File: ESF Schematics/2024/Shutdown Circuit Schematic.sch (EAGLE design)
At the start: 32 parts, among them J1 CONNECTOR-1_6MM2, J10 CONNECTOR-1_CT2242-2, J11 CONNECTOR-3_XXC106-EV-P3Z, J15 CONNECTOR-3_NEMA-5-20, J16 CONNECTOR-3_NEMA-5-20, J17 CONNECTOR-2_, J18 CONNECTOR-2_, J2 CONNECTOR-1_LCAX2-14F-E, J3 CONNECTOR-1_6MM2, J4 CONNECTOR-1_LCAX2-14F-E, J5 CONNECTOR-3_XXC106-EV-P3Z, J6 RING_TERMINAL_19054-0042, J7 RING_TERMINAL_19054-0042, J8 CONNECTOR-3_NEMA-5-20, J9 CONNECTOR-1_CT2242-2

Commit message: num num
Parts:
- removed A1: REMOTE_POWER_CONTROL_RPC-20-SCD, HyTechSymbolsTemp:REMOTE_POWER_CONTROL_RPC-20-SCD
- removed A2: CHARGER_HK-J-H650-12, HyTechSymbols:CHARGER_HK-J-H650-12
- removed A3: INLINE_GFCI_GFM20-3WC, HyTechSymbolsTemp:INLINE_GFCI_GFM20-3WC
- removed F4: 1A, HyTechSymbolsTemp:FUSE
- removed J10, J9: CONNECTOR-1_CT2242-2, HyTechSymbolsTemp:CONNECTOR-1_CT2242-2
- removed J11, J5: CONNECTOR-3_XXC106-EV-P3Z, HyTechSymbols:CONNECTOR-3_XXC106-EV-P3Z
- removed J15, J16, J8: CONNECTOR-3_NEMA-5-20, HyTechSymbolsTemp:CONNECTOR-3_NEMA-5-20
- removed J17, J18: CONNECTOR-2_, HyTechSymbols:CONNECTOR-2_XXC104-EV-P1ZA
- removed J2, J4: CONNECTOR-1_LCAX2-14F-E, HyTechSymbols:CONNECTOR-1_LCAX2-14F-E
- removed J3: CONNECTOR-1_6MM2, HyTechSymbols:CONNECTOR-1_6MM2
- removed J6, J7: RING_TERMINAL_19054-0042, HyTechSymbols:RING_TERMINAL_19054-0042
- removed R1: 15k, HyTechSymbolsTemp:RESISTOR
- removed U$7: RING_TERMINAL_19054-0042, HyTechSymbolsTemp:RING_TERMINAL_19054-0042
- added AIR+, AIR-: RELAY_SPST_NO_, HyTechSymbols:RELAY_SPST_NO_
- added AMS_RELAY, BOTS_SENSE_RELAY, BSPD_RELAY, IMD_RELAY, SOFTWARE_SHDN_RELAY: RELAY_DPDT_RT424024, HyTechSymbols:RELAY_DPDT_RT424024
- added D1, D10, D2, D3, D4, D5, D6, D7, D8, D9: DIODE, HyTechSymbolsTemp:DIODE
- added DISCHARGE: RELAY_SPST_NC_DBR72410, HyTechSymbols:RELAY_SPST_NC_DBR72410
- added DISCHARGE_RES, DISCHARGE_RES1, DISCHARGE_RES2: 15k, HyTechSymbolsTemp:RESISTOR
- added F1: 10A, HyTechSymbolsTemp:FUSE
- added F6: 1A, HyTechSymbolsTemp:FUSE
- added GLV_BATTERY: BATTERY, HyTechSymbols:BATTERY
- added LATCHING_BUTTON: BUTTON_NO_LP9, HyTechSymbolsTemp:BUTTON_NO_LP9
- added MAIN_FUSE: 125A, HyTechSymbolsTemp:FUSE
- added PACK+OPTOISOLATOR: RELAY_SOLIDSTATE_NO_, HyTechSymbolsTemp:RELAY_SOLIDSTATE_NO_
- added PRECHARGE: RELAY_SPST_NO_DAR72410, HyTechSymbols:RELAY_SPST_NO_DAR72410
- added PRECHARGE_RES, PRECHARGE_RES1: 1.5k, HyTechSymbolsTemp:RESISTOR
- added Q1, Q2: MOSFET_N-CHANNEL, HyTechSymbolsTemp:MOSFET_N-CHANNEL
- added R3: 3.3k, HyTechSymbolsTemp:RESISTOR
- added S10, S11, S12, S13, S6, S7: SWITCH_SPST_, HyTechSymbols:SWITCH_SPST_
- added S3: SWITCH_SPST_27MM_STOP, HyTechSymbols:SWITCH_SPST_27MM_STOP
- added S4, S5: SWITCH_SPST_40MM_STOP, HyTechSymbols:SWITCH_SPST_40MM_STOP
- added S8, S9: SWITCH_SPST_35-210-100-R-900, HyTechSymbols:SWITCH_SPST_35-210-100-R-900
- added U$10: BENDER_IR155-3204, HyTechSymbols:BENDER_IR155-3204
- added U$12, U$13, U$14: SEGMENT, HyTechSymbols:SEGMENT
- added U$17: PRECHARGER, HyTechSymbolsTemp:PRECHARGER
- added U$2, U$20, U$21, U$22, U$23, U$24, U$25, U$34, U$35, U$36, U$37: MAINTENANCE_PLUG_104742-2, HyTechSymbolsTemp:MAINTENANCE_PLUG_104742-2
- added U$38, U$39, U$40: RING_TERMINAL_19054-0042, HyTechSymbolsTemp:RING_TERMINAL_19054-0042
- added U1, U2: LOGICGATE_INVERTER, HyTechSymbolsTemp:LOGICGATE_INVERTER
- F3: value 175A -> 3A
- J1: value CONNECTOR-1_6MM2 -> CONNECTOR-2_HVP800; device HyTechSymbols:CONNECTOR-1_6MM2 -> HyTechSymbols:CONNECTOR-2_HVP800
- R2: value 15k -> 39
- S1: value SWITCH_SPST_ -> SWITCH_SPST_INERTIA_SWITCH; device HyTechSymbols:SWITCH_SPST_ -> HyTechSymbols:SWITCH_SPST_INERTIA_SWITCH; MPN AIR+ -> (none)
- S2: MPN AIR- -> BOTS
- U$1, U$4: value CONNECTOR-2_HVP800 -> SEGMENT; device HyTechSymbols:CONNECTOR-2_HVP800 -> HyTechSymbols:SEGMENT
- U$15: value CHARGER_CONTROLLER -> SEGMENT; device HyTechSymbolsTemp:CHARGER_CONTROLLER -> HyTechSymbols:SEGMENT
- U$3: value CONNECTOR-3_XXC106-EV-P3Z -> MAINTENANCE_PLUG_104742-2; device HyTechSymbols:CONNECTOR-3_XXC106-EV-P3Z -> HyTechSymbolsTemp:MAINTENANCE_PLUG_104742-2
- U$5: value BENDER_IR155-3204 -> MAINTENANCE_PLUG_104742-2; device HyTechSymbols:BENDER_IR155-3204 -> HyTechSymbolsTemp:MAINTENANCE_PLUG_104742-2
- U$6: value RING_TERMINAL_19054-0042 -> MAINTENANCE_PLUG_104742-2; device HyTechSymbolsTemp:RING_TERMINAL_19054-0042 -> HyTechSymbolsTemp:MAINTENANCE_PLUG_104742-2
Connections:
- removed net CHARGER_CONTROLLER_CANH: A2.CANH, U$15.CANH
- removed net CHARGER_CONTROLLER_CANL: A2.CANL, U$15.CANL
- removed net N$22 (its old number): A1.HOTIN, J15.1
- removed net N$27: R2.1, U$6.P$2
- removed net N$28: A3.HOT_OUT, J8.1
- removed net N$30: A3.GND_IN, J16.3
- removed net OKHS: U$5.OKHS
- new net +5V: U$17.VDD
- new net AMS_OK: AMS_RELAY.COIL+, D7.C
- new net BOTS_SENSE: BOTS_SENSE_RELAY.COIL+, D2.C, IMD_RELAY.6, S2.O
- new net BSPD_OK: BSPD_RELAY.COIL+, D9.C
- new net GLV_SYSTEMS: F3.1, S9.S
- new net IMD_OK: D10.C, IMD_RELAY.COIL+, U$10.OKHS
- new net N$12: S4.O, S5.P
- new net N$13: S5.O, S7.P
- new net N$16: BOTS_SENSE_RELAY.3, BOTS_SENSE_RELAY.COIL-, D1.A, D2.A
- new net N$17: S12.P, S13.S
- new net N$18: S1.O, S11.P
- new net N$34: U$14.+, U$23.1
- new net N$36: U$15.+, U$25.1
- new net N$37: U$34.P$1, U$35.P$1
- new net N$38: AIR+.CONTACT2, U$34.1
- new net N$39: PACK+OPTOISOLATOR.CONTROL+, R3.1
- new net N$40: PACK+OPTOISOLATOR.CONTACT1, R2.2
- new net N$42: BSPD_RELAY.5, SOFTWARE_SHDN_RELAY.6
- new net N$43: U$20.P$1, U$21.P$1
- new net N$44: U$22.P$1, U$23.P$1
- new net N$45: U$24.P$1, U$25.P$1
- new net N$46: U$36.P$1, U$37.P$1
- new net N$47: AIR-.CONTACT1, U$37.1
- new net N$48: F6.2, U$38.P$1
- new net N$50: F5.2, U$39.P$1
- new net N$51: S6.P, S7.S
- new net N$52: Q2.G, U2.!IN
- new net N$53: AIR+.COIL+, Q2.D
- new net N$54: U$1.+, U$3.1
- new net N$55: U$2.P$1, U$3.P$1
- new net N$56: U$36.1, U$4.-
- new net N$57: U$4.+, U$6.1
- new net N$58: U$5.P$1, U$6.P$1
- new net N$59: S12.S, S3.P
- new net PACK+: PACK+OPTOISOLATOR.CONTACT2, PRECHARGE.CONTACT1, U$12.+, U$35.1, U$40.P$2
- new net PACK+FUSED: R2.1, U$17.PACK+
- new net PRECHARGE_OK: PRECHARGE.COIL+, Q1.D, U1.IN
- new net SOFTWARE_OK: D8.C, SOFTWARE_SHDN_RELAY.COIL+
- new net TS+UNFUSED: AIR+.CONTACT1, DISCHARGE.CONTACT1, J1.1, PRECHARGE_RES.2, PRECHARGE_RES1.2
- net +12V: now also U$10.+12V; no longer U$5.+12V
- net GND: now also AIR-.COIL+, AMS_RELAY.4, BOTS_SENSE_RELAY.4, DISCHARGE.COIL-, GLV_BATTERY.P$2, IMD_RELAY.4, LATCHING_BUTTON.P$1, PACK+OPTOISOLATOR.CONTROL-, Q1.S, Q2.S, SOFTWARE_SHDN_RELAY.4, U$10.GND, U$17.GND; no longer U$5.GND
- net N$1: now also D10.A, D6.A, IMD_RELAY.3, IMD_RELAY.COIL-; no longer A2.NEUTRAL, U$3.2
- net N$10: now also AMS_RELAY.5, BSPD_RELAY.6; no longer S1.P, U$1.1
- net N$11: now also AMS_RELAY.6, IMD_RELAY.5; no longer F3.1, U$1.2
- net N$14: now also F1.1, GLV_BATTERY.P$1; no longer J1.1, J18.1
- net N$15: now also BOTS_SENSE_RELAY.6, SOFTWARE_SHDN_RELAY.5; no longer J18.2, J3.1
- net N$19: now also BOTS_SENSE_RELAY.5, S13.P; no longer A1.GND_OUT, J5.3
- net N$2: now also D1.C, D3.C, D4.C, D5.C, D6.C, LATCHING_BUTTON.P$2; no longer A2.GND, U$3.3
- net N$20: now also S10.P, S11.S; no longer J4.1, U$4.2
- net N$21: now also S6.S, S8.P; no longer J2.1, U$4.1
- net N$23: now also U$1.-, U$5.1; no longer A3.NEUTRAL_OUT, J8.2
- net N$24: now also Q1.G, U1.!IN; no longer A1.NEUTRAL_IN, J15.2
- net N$25: now also U$17.PRECHARGE_OK, U2.IN; no longer R1.1, U$7.P$2
- net N$26: now also PRECHARGE.CONTACT2, PRECHARGE_RES.1, PRECHARGE_RES1.1; no longer F5.2, J7.P$2
- net N$29: now also DISCHARGE.CONTACT2, DISCHARGE_RES.1, DISCHARGE_RES1.1, DISCHARGE_RES2.1; no longer A3.GND_OUT, J8.3
- net N$3: now also AMS_RELAY.3, AMS_RELAY.COIL-, D5.A, D7.A; no longer A2.HOT, U$3.1
- net N$31: now also U$12.-, U$20.1; no longer A3.NEUTRAL_IN, J16.2
- net N$32: now also U$13.+, U$21.1; no longer A3.HOTIN, J16.1
- net N$33: now also U$13.-, U$22.1; no longer A1.GND_IN, J15.3
- net N$35: now also U$14.-, U$24.1; no longer F4.2, J6.P$2
- net N$4: now also S10.S, S4.P; no longer J17.1
- net N$5: now also D4.A, D8.A, SOFTWARE_SHDN_RELAY.3, SOFTWARE_SHDN_RELAY.COIL-; no longer A2.TS-, J17.2
- net N$6: now also BSPD_RELAY.3, BSPD_RELAY.COIL-, D3.A, D9.A; no longer A1.HOT_OUT, J5.1
- net N$7: now also F1.2, S9.P; no longer A1.NEUTRAL_OUT, J5.2
- net N$8: now also S1.P, S3.O; no longer J9.1, R1.2
- net N$9: now also U$15.-, U$2.1; no longer J10.1, R2.2
- net SHDN: now also AIR+.COIL-, AIR-.COIL-, DISCHARGE.COIL+, PRECHARGE.COIL-, R3.2, S8.S; no longer A1.EN
- net TS+: now also F5.1, U$10.XLA+(HV+), U$17.TS+; no longer F4.1, U$5.XLA+(HV+)
- net TS-UNFUSED: now also AIR-.CONTACT2, DISCHARGE_RES.2, DISCHARGE_RES1.2, DISCHARGE_RES2.2, F6.1, J1.2, MAIN_FUSE.1, MAIN_FUSE.2, U$10.XLA-(HV-), U$17.TS-; no longer F5.1, U$5.XLA-(HV-)
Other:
- note added: "(>= 6 mil)"
- note added: "(Busbar)"
- note added: "16AWG"
- note added: "16AWG:"
- note added: "Cockpit BRB"
- note added: "ESF compliant reresentation of the HT08"
- note added: "GLVMS"
- note added: "Inertia Switch"
- note added: "Inverter Enclosure"
- note added: "Left BRB"
- note added: "PCB Trace"
- note added: "PCB Trace:"
- note added: "Right BRB"
- note added: "Shayan Noorani"
- note added: "TSMS"
- note removed: "12AWG"
- note removed: "12AWG:"
- note removed: "35mm^2"
- note removed: "35mm^2:"
- note removed: "6mm^2"
- note removed: "6mm^2:"
- note removed: "Charger TSMPs"
- note removed: "To external AC Power"
- moved on the sheet: F3, F5, R2

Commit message: getting this done edited the shutdown
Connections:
- net N$18: now also S3.P; no longer S11.P
- net N$59: now also S1.P; no longer S3.P
- net N$8: now also S11.P; no longer S1.P
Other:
- note added: "Shayan Noorani & Liwei Sun"
- note removed: "Shayan Noorani"
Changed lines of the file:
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@@
 <text x="76.2" y="142.24" size="1.27" layer="97" align="top-left">22AWG</text>
 <text x="208.28" y="208.28" size="1.27" layer="97" align="top-left">PCB Trace</text>
-<text x="200.66" y="142.24" size="1.27" layer="97" align="top-left">22AWG</text>
+<text x="218.44" y="142.24" size="1.27" layer="97" align="top-left">22AWG</text>
 <text x="22.86" y="96.52" size="1.27" layer="97" align="top-left">22AWG</text>
 <text x="27.94" y="12.7" size="1.27" layer="97" align="top-left">22AWG</text>
@@
 <text x="124.46" y="144.78" size="1.27" layer="97" align="bottom-center">Right BRB</text>
 <text x="142.24" y="144.78" size="1.27" layer="97" align="bottom-center">Left BRB</text>
-<text x="213.36" y="144.78" size="1.27" layer="97" align="bottom-center">Cockpit BRB</text>
-<text x="195.58" y="144.78" size="1.27" layer="97" align="bottom-center">Inertia Switch</text>
+<text x="195.58" y="144.78" size="1.27" layer="97" align="bottom-center">Cockpit BRB</text>
+<text x="213.36" y="144.78" size="1.27" layer="97" align="bottom-center">Inertia Switch</text>
 <text x="17.78" y="170.18" size="1.27" layer="97" align="top-left">16AWG</text>
 <text x="91.44" y="142.24" size="1.27" layer="97" align="top-left">22AWG</text>
@@
 <text x="147.32" y="142.24" size="1.27" layer="97" align="top-left">22AWG</text>
 <text x="109.22" y="142.24" size="1.27" layer="97" align="top-left">22AWG</text>
-<text x="218.44" y="142.24" size="1.27" layer="97" align="top-left">22AWG</text>
+<text x="200.66" y="142.24" size="1.27" layer="97" align="top-left">22AWG</text>
 <text x="60.96" y="160.02" size="1.27" layer="97" rot="R180" align="top-left">22AWG</text>
 <text x="167.64" y="142.24" size="1.27" layer="97" align="top-left">22AWG</text>
@@
 Connection</text>
 <text x="198.12" y="15.24" size="2.54" layer="95">ESF compliant reresentation of the HT08 </text>
-<text x="134.62" y="22.86" size="2.54" layer="95">Shayan Noorani</text>
-<text x="177.8" y="30.48" size="2.54" layer="95">Shayan Noorani</text>
+<text x="128.27" y="22.352" size="2.54" layer="95">Shayan Noorani &amp; Liwei Sun</text>
 </plain>
 <instances>
@@
 <attribute name="VALUE" x="252.73" y="115.57" size="1.27" layer="96" align="top-center"/>
 </instance>
-<instance part="S1" gate="SPST" x="195.58" y="139.7" smashed="yes" rot="MR0">
-<attribute name="MANUFACTURER" x="195.58" y="143.002" size="1.27" layer="96" rot="MR0" align="bottom-center"/>
-<attribute name="MPN" x="195.58" y="136.398" size="1.27" layer="96" rot="MR0" align="top-center"/>
+<instance part="S1" gate="SPST" x="213.36" y="139.7" smashed="yes" rot="MR0">
+<attribute name="MANUFACTURER" x="213.36" y="143.002" size="1.27" layer="96" rot="MR0" align="bottom-center"/>
+<attribute name="MPN" x="213.36" y="136.398" size="1.27" layer="96" rot="MR0" align="top-center"/>
 </instance>
 <instance part="S2" gate="SPST" x="60.96" y="162.56" smashed="yes" rot="MR180">
@@
 <attribute name="MPN" x="60.96" y="165.862" size="1.27" layer="96" rot="MR180" align="top-center"/>
 </instance>
-<instance part="S3" gate="SPST" x="213.36" y="139.7" smashed="yes" rot="MR0">
-<attribute name="MANUFACTURER" x="213.36" y="143.002" size="1.27" layer="96" rot="MR0" align="bottom-center"/>
-<attribute name="MPN" x="213.36" y="136.398" size="1.27" layer="96" rot="MR0" align="top-center"/>
+<instance part="S3" gate="SPST" x="195.58" y="139.7" smashed="yes" rot="MR0">
+<attribute name="MANUFACTURER" x="195.58" y="143.002" size="1.27" layer="96" rot="MR0" align="bottom-center"/>
+<attribute name="MPN" x="195.58" y="136.398" size="1.27" layer="96" rot="MR0" align="top-center"/>
 </instance>
 <instance part="S4" gate="SPST" x="142.24" y="139.7" smashed="yes" rot="MR0">
@@
 <segment>
 <pinref part="S3" gate="SPST" pin="O"/>
-<wire x1="208.28" y1="139.7" x2="208.28" y2="142.24" width="0.1524" layer="91"/>
-<pinref part="S1" gate="SPST" pin="P"/>
-<wire x1="200.66" y1="139.7" x2="208.28" y2="139.7" width="0.1524" layer="91"/>
+<wire x1="190.5" y1="139.7" x2="190.5" y2="142.24" width="0.1524" layer="91"/>
+<pinref part="S11" gate="SPST" pin="P"/>
+<wire x1="185.42" y1="139.7" x2="190.5" y2="139.7" width="0.1524" layer="91"/>
 </segment>
 </net>
@@
 <wire x1="269.24" y1="73.66" x2="259.08" y2="73.66" width="0.4445" layer="91"/>
 <wire x1="269.24" y1="53.34" x2="269.24" y2="73.66" width="0.4445" layer="91"/>
-<label x="259.08" y="76.2" size="1.27" layer="95"/>
+<label x="259.08" y="74.422" size="1.27" layer="95"/>
 <wire x1="119.38" y1="53.34" x2="269.24" y2="53.34" width="0.4445" layer="91"/>
 <pinref part="MAIN_FUSE" gate="G$1" pin="2"/>
@@
 <net name="N$59" class="0">
 <segment>
-<pinref part="S3" gate="SPST" pin="P"/>
-<wire x1="228.6" y1="139.7" x2="218.44" y2="139.7" width="0.1524" layer="91"/>
 <pinref part="S12" gate="SPST" pin="S"/>
 <wire x1="228.6" y1="139.7" x2="228.6" y2="137.16" width="0.1524" layer="91"/>
+<pinref part="S1" gate="SPST" pin="P"/>
+<wire x1="218.44" y1="139.7" x2="228.6" y2="139.7" width="0.1524" layer="91"/>
 </segment>
 </net>
@@
 <net name="N$18" class="0">
 <segment>
-<pinref part="S11" gate="SPST" pin="P"/>
-<wire x1="185.42" y1="139.7" x2="190.5" y2="139.7" width="0.1524" layer="91"/>
 <pinref part="S1" gate="SPST" pin="O"/>
-<wire x1="190.5" y1="139.7" x2="190.5" y2="142.24" width="0.1524" layer="91"/>
-</segment>
-</net>
+<wire x1="208.28" y1="139.7" x2="208.28" y2="142.24" width="0.1524" layer="91"/>
+<pinref part="S3" gate="SPST" pin="P"/>
+<wire x1="200.66" y1="139.7" x2="208.28" y2="139.7" width="0.1524" layer="91"/>
+</segment>
+</net>

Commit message: fixing broken stuff
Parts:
- F1: value 10A -> 15A; device HyTechSymbolsTemp:FUSE -> HyTechSymbols:FUSE
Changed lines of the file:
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@@
 <part name="P3" library="HyTechSupplies" deviceset="GND" device=""/>
 <part name="BSPD_RELAY" library="HyTechSymbols" deviceset="RELAY_DPDT_?*" device="" technology="RT424024" value="RELAY_DPDT_RT424024"/>
-<part name="F1" library="HyTechSymbolsTemp" deviceset="FUSE" device="" value="10A"/>
+<part name="F1" library="HyTechSymbols" deviceset="FUSE" device="" value="15A"/>
 <part name="F3" library="HyTechSymbolsTemp" deviceset="FUSE" device="" value="3A"/>
 <part name="U$10" library="HyTechSymbols" deviceset="BENDER_IR155-3204" device=""/>

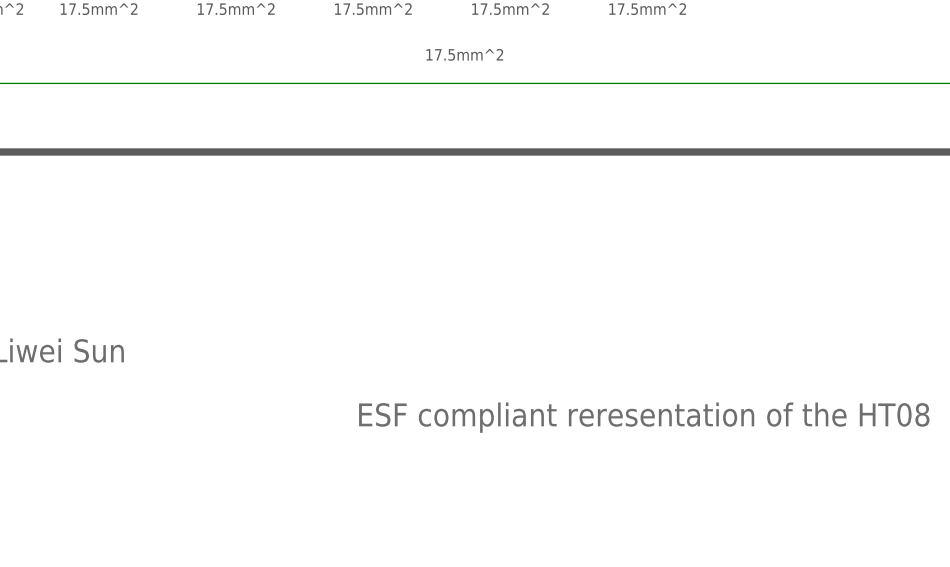
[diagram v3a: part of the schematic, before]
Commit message: added reviewer names
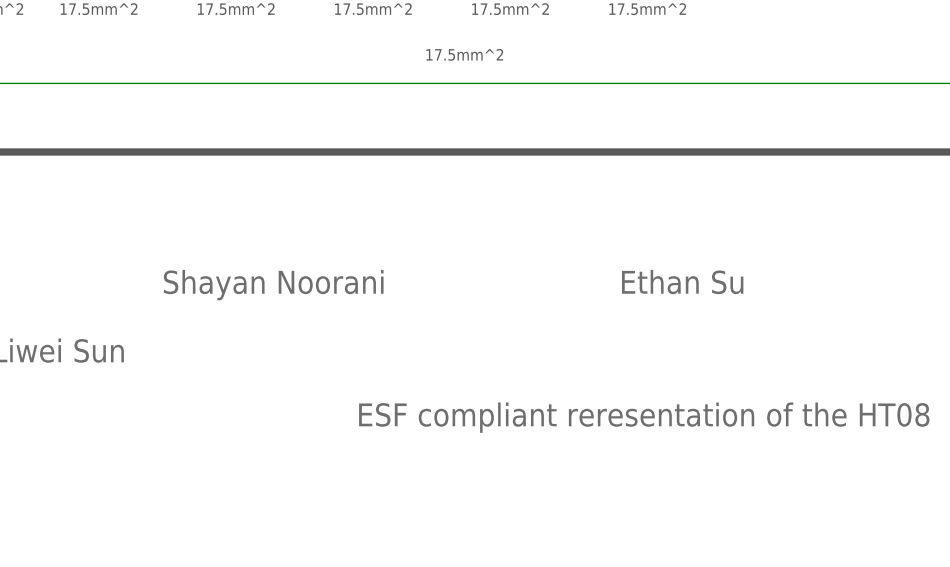
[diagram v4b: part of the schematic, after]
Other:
- note added: "Ethan Su"
- note added: "Shayan Noorani"
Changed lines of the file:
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@@
 <text x="198.12" y="15.24" size="2.54" layer="95">ESF compliant reresentation of the HT08 </text>
 <text x="128.27" y="22.352" size="2.54" layer="95">Shayan Noorani &amp; Liwei Sun</text>
+<text x="176.53" y="29.972" size="2.54" layer="95">Shayan Noorani</text>
+<text x="227.33" y="29.972" size="2.54" layer="95">Ethan Su</text>
 </plain>
 <instances>
